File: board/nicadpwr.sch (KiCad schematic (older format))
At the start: 35 parts, among them P1 CONN_SENSE, P2 CONN_CHARGE, P3 CONN_BAT, P4 CONN_VOUT, Q1 Si4562DY, Q2 BC547, Q3 Si4562DY, U1 LM317T, U2 LM1117-5.0, U3 MC34063A

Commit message: Rdesign of the board for v3
The new version moves boost converter and charger out
of the main path to be active only when charging.
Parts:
- removed C3: 10uF, Capacitors_SMD:C_0805_HandSoldering, symbol C
- removed C5: 22uF, Capacitors_Tantalum_SMD:CP_Tantalum_Case-X_EIA-7343-43_Wave, symbol C
- removed C6: 100nF, Capacitors_SMD:C_0603_HandSoldering, symbol C
- removed U2: LM1117-5.0, TO_SOT_Packages_SMD:SOT-223, symbol LM1117-5.0
- C4: value 1nF -> 700pF
- C7: value 470uF -> 1000uF
- R1: value 100 -> 330K
- R2: value 47K -> 100
- R3: value 100K -> 47K
- R5: value 100K -> 330K
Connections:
- net BOOST_IN: now also Q3.5 (D2), Q3.6 (D2); no longer D1.1 (K), Q1.5 (D2), Q1.6 (D2)
- net BOOST_OUT: now also C2.1, R2.2, U1.3 (IN); no longer Q3.3 (S2), R11.1
- net Earth: no longer R2.2
- net VBAT: no longer Q1.7 (D1), Q1.8 (D1)
- net VCHARGE: no longer C1.1, R1.2
- net VOUT: now also C1.1, D1.1 (K), Q1.5 (D2), Q1.6 (D2), Q3.3 (S2), R11.1
- net at R5.2, R6.1, U3.5 (COMP): now also R1.2
- net at D6.1 (K), R5.1: now also R1.1
- net at Q1.4 (G2), R3.1: now also R2.1; no longer Q1.1 (S1)
- removed net CHARGE_IN: C2.1, Q3.5 (D2), Q3.6 (D2), U1.3 (IN)
- now unconnected: Q1.2 (G1)
- no-connect marks 0 -> 5
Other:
- note removed: "TODO: Put Cap after diode"
- note removed: "This pulldown isnt needed. R2 does the job"

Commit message: Fixes in schematic only to match working version:
1. Boost capacitor was reduced to 220uF
2. Control signal of the VBAT-VOUT switch was changed
  to VCHARGE instead of BOOST_OUT. The problem with the
  latter is discharge time of the boost cap.
3. Led was removed since it was not populated in the working board.
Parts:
- removed D5: LED, LEDs:LED_0805_HandSoldering, symbol LED
- removed R8: 200, Resistors_SMD:R_0805_HandSoldering, symbol R
- C7: value 1000uF -> 220uF
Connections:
- net BOOST_OUT: no longer R2.2
- net VCHARGE: now also R2.2
- no-connect marks 5 -> 4

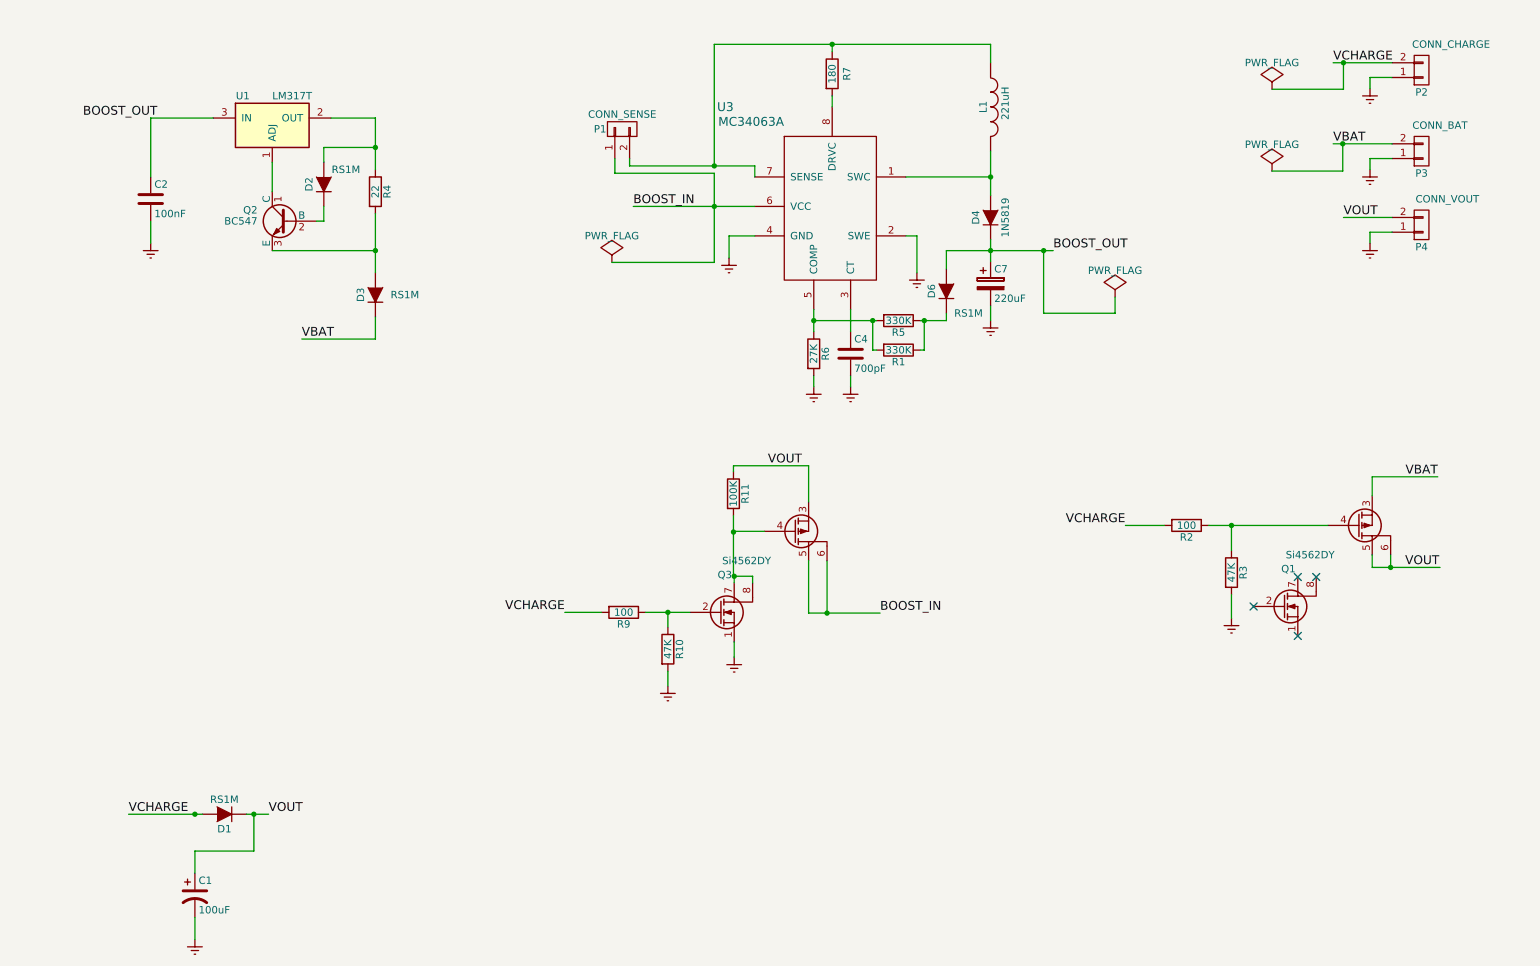
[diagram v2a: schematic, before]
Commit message: Fix bugs to finaly get working board ...
1. Upper rail for the sense opamp was set to +4V which holds its
output under 1V. This is not enough for control of the MSP which
is expected to be around 1.25V. Changed the upper rail to BOOST_OUT.

2. Signal controlling Q1 battery switch was connected to BOOST_OUT.
This works, but when charger is disconnected boost out capaccitor
discharges relatively slowly and opens Q1 with considerable delay.
Changed the Q1 control to VCHARGE instead.
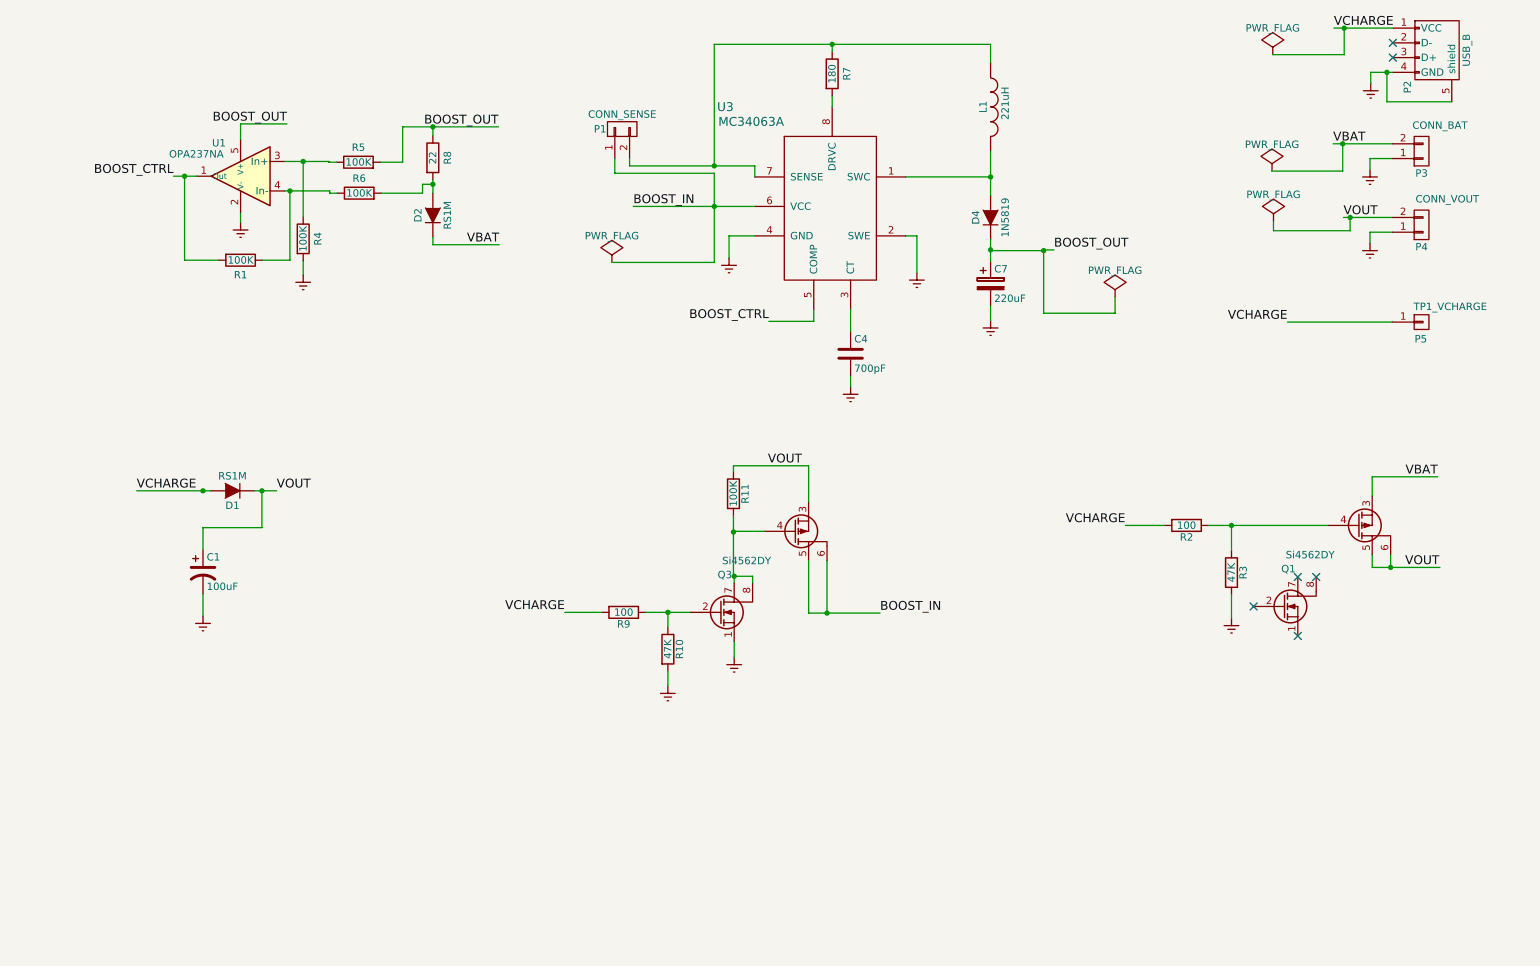
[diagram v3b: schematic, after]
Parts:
- removed C2: 100nF, Capacitors_SMD:C_0603_HandSoldering, symbol C
- removed D3, D6: RS1M, Diodes_SMD:D_SMA_Handsoldering, symbol D
- removed P2: CONN_CHARGE, Socket_Strips:Socket_Strip_Straight_1x02_Pitch2.54mm, symbol CONN_01X02
- removed Q2: BC547, TO_SOT_Packages_THT:TO-92_Molded_Wide_Oval, symbol BC547
- removed U1: LM317T, nicadpwr:LM317T-TO220, symbol LM317T
- added P2: USB_B, Connect:USB_Mini-B, symbol USB_B
- added P5: TP1_VCHARGE, Connect:Pin_d0.9mm_L10.0mm_W2.4mm_FlatFork, symbol CONN_01X01
- added R8: 22, Resistors_SMD:R_0805_HandSoldering, symbol R
- added U1: OPA237NA, TO_SOT_Packages_SMD:SOT-23-5_HandSoldering, symbol OPA237NA
- C7: footprint Capacitors_ThroughHole:CP_Radial_D10.0mm_P5.00mm -> Capacitors_ThroughHole:CP_Radial_D6.3mm_P2.50mm
- R1, R5: value 330K -> 100K
- R4: value 22 -> 100K
- R6: value 27K -> 100K
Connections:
- net BOOST_OUT: now also R5.2, R8.1, U1.5 (V+)
- net Earth: now also R4.2, P2.4 (GND), P2.5 (shield), U1.2 (V-); no longer R6.2
- net VBAT: now also D2.1 (K)
- net VCHARGE: now also P2.1 (VCC), P5.1 (P1)
- net at D2.2 (A): now also R6.2, R8.2; no longer R4.1
- net BOOST_CTRL: now reaches R1.2, U3.5 (COMP)
- net BOOST_CTRL: now also U1.1 (Out); no longer R5.2, R6.1
- net at R5.1: now also R4.1, U1.3 (In+); no longer R1.1
- new net: R1.1, R6.1, U1.4 (In-)
- no-connect marks 4 -> 6
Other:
- moved on the sheet: C1, D1
